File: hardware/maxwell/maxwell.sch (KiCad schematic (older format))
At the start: 48 parts, among them J1 Canbus 1, J10 SPI2_B, J11 BACKUP, J12 UART4, J15 I2C1, J16 ESP_BM, J17 ESP_PROG, J2 SPI2_C, J20 Interconnect (uC), J3 Neopixel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

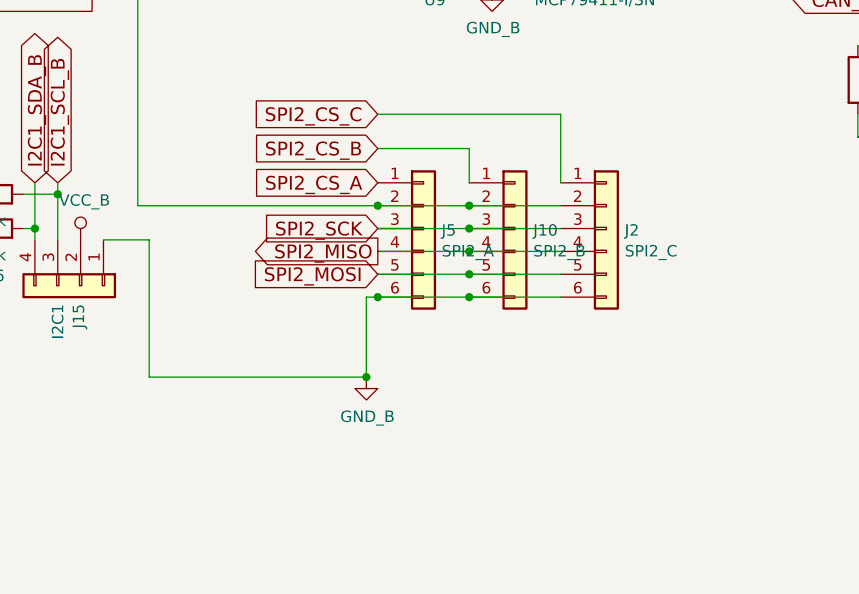
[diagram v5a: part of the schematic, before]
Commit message: Maxwell v1.9.6
Adapting main uC board such that it can serve for _both_ the
remote and main sides.  I'm printing a new case that can be mounted on
the front rack of the bike instead of the rear; this would obviate the
need for having two separate microcontrollers communicating over CAN.

* Adds new DISP connector in place of SPI_C (currently unused).
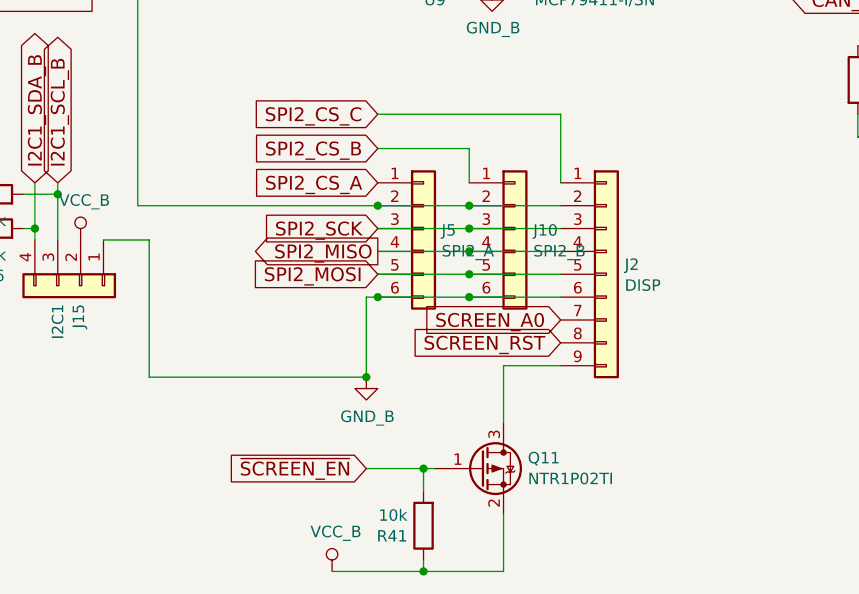
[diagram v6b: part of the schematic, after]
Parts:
- removed J2: SPI2_C, coddingtonbear:JST_XH_B06B-XH-A_06x2.50mm_Straight_LargePads, symbol maxwell-rescue:Conn_01x06-conn
- added J2: DISP, coddingtonbear:JST_XH_B09B-XH-A_1x09_P2.50mm_Straight_LargePads, symbol Connector_Generic:Conn_01x09
- added Q11: NTR1P02TI, coddingtonbear:SOT-23_LargePads, symbol Device:Q_PMOS_GSD
- added R41: 10k, coddingtonbear:0805_Milling, symbol maxwell-rescue:R-RESCUE-maxwell
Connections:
- net GND_B: now also J2.6 (Pin_6)
- net SPI2_CS_C: now also J2.1 (Pin_1)
- net SPI2_MISO: now also J2.4 (Pin_4)
- net SPI2_MOSI: now also J2.5 (Pin_5)
- net SPI2_SCK: now also J2.3 (Pin_3)
- net VCC_B: now also Q11.2 (S), R41.1
- net at J10.2 (Pin_2), J5.2 (Pin_2), U21.1 (DRAIN)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: now also J2.2 (Pin_2)
- new net: J2.9 (Pin_9), Q11.3 (D)
- new net SCREEN_A0: J2.7 (Pin_7)
- new net SCREEN_RST: J2.8 (Pin_8)
- new net ~SCREEN_EN: Q11.1 (G), R41.2
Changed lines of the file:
@@
 NoConn ~ 9450 3350
 NoConn ~ 9550 3350
-$Comp
-L maxwell-rescue:Conn_01x06-conn J2
-U 1 1 5BFB23A5
-P 6350 5500
-F 0 "J2" H 6430 5492 50  0000 L CNN
-F 1 "SPI2_C" H 6430 5401 50  0000 L CNN
-F 2 "coddingtonbear:JST_XH_B06B-XH-A_06x2.50mm_Straight_LargePads" H 6350 5500 50  0001 C CNN
-F 3 "~" H 6350 5500 50  0001 C CNN
-	1    6350 5500
-	1    0    0    -1
-$EndComp
 Wire Wire Line
 	5750 5400 6150 5400
@@
 Wire Wire Line
 	4600 3750 4600 4150
+$Comp
+L Connector_Generic:Conn_01x09 J2
+U 1 1 5CC5BE53
+P 6350 5700
+F 0 "J2" H 6430 5742 50  0000 L CNN
+F 1 "DISP" H 6430 5651 50  0000 L CNN
+F 2 "coddingtonbear:JST_XH_B09B-XH-A_1x09_P2.50mm_Straight_LargePads" H 6350 5700 50  0001 C CNN
+F 3 "~" H 6350 5700 50  0001 C CNN
+	1    6350 5700
+	1    0    0    -1
+$EndComp
+Text GLabel 6150 5900 0    60   Input ~ 0
+SCREEN_A0
+Text GLabel 6150 6000 0    60   Input ~ 0
+SCREEN_RST
+$Comp
+L Device:Q_PMOS_GSD Q11
+U 1 1 5CC5E136
+P 5800 6550
+F 0 "Q11" H 6006 6596 50  0000 L CNN
+F 1 "NTR1P02TI" H 6006 6505 50  0000 L CNN
+F 2 "coddingtonbear:SOT-23_LargePads" H 6000 6650 50  0001 C CNN
+F 3 "~" H 5800 6550 50  0001 C CNN
+	1    5800 6550
+	1    0    0    -1
+$EndComp
+Text GLabel 5300 6550 0    60   Input ~ 0
+~SCREEN_EN
+$Comp
+L maxwell-rescue:R-RESCUE-maxwell R41
+U 1 1 5CC5F256
+P 5550 6800
+F 0 "R41" H 5620 6846 50  0000 L CNN
+F 1 "10k" H 5620 6755 50  0000 L CNN
+F 2 "coddingtonbear:0805_Milling" V 5480 6800 50  0001 C CNN
+F 3 "" H 5550 6800 50  0001 C CNN
+	1    5550 6800
+	-1   0    0    1
+$EndComp
+Wire Wire Line
+	5900 6750 5900 7000
+Wire Wire Line
+	5900 7000 5550 7000
+Wire Wire Line
+	5600 6550 5550 6550
+Wire Wire Line
+	5550 6650 5550 6550
+Connection ~ 5550 6550
+Wire Wire Line
+	5550 6550 5300 6550
+Wire Wire Line
+	5550 6950 5550 7000
+Connection ~ 5550 7000
+Wire Wire Line
+	5550 7000 5150 7000
+Wire Wire Line
+	6150 6100 5900 6100
+Wire Wire Line
+	5900 6100 5900 6350
+$Comp
+L coddingtonbear:VCC_B #PWR?
+U 1 1 5CCA1B6F
+P 5150 7000
+F 0 "#PWR?" H 5150 6850 50  0001 C CNN
+F 1 "VCC_B" H 5167 7173 50  0000 C CNN
+F 2 "" H 5150 7000 50  0001 C CNN
+F 3 "" H 5150 7000 50  0001 C CNN
+	1    5150 7000
+	1    0    0    -1
+$EndComp
 $EndSCHEMATC

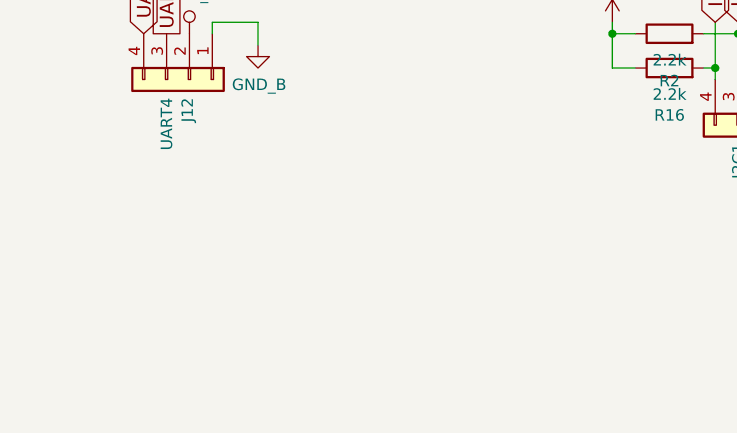
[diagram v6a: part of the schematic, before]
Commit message: Maxwell v1.9.7
Forgot to add connectors for left/right control sets.

* Adds connectors for LEFT_A/B and RIGHT_A/B
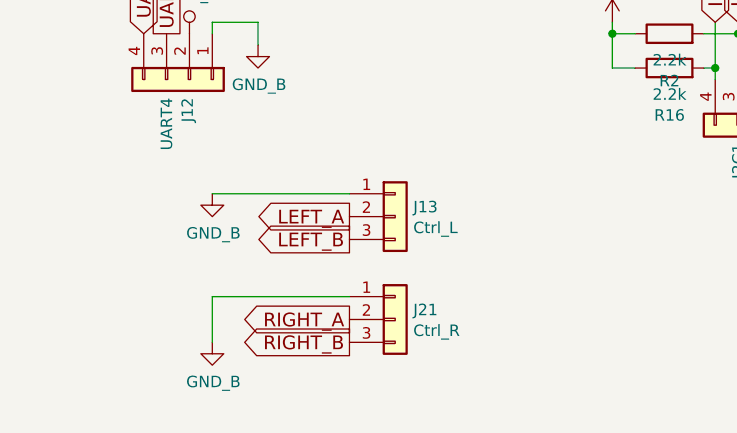
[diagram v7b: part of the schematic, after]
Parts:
- added J13: Ctrl_L, coddingtonbear:JST_XH_B03B-XH-A_03x2.50mm_Straight_LargePads, symbol Connector_Generic:Conn_01x03
- added J21: Ctrl_R, coddingtonbear:JST_XH_B03B-XH-A_03x2.50mm_Straight_LargePads, symbol Connector_Generic:Conn_01x03
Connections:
- net GND_B: now also J13.1 (Pin_1), J21.1 (Pin_1)
- new net LEFT_A: J13.2 (Pin_2)
- new net LEFT_B: J13.3 (Pin_3)
- new net RIGHT_A: J21.2 (Pin_2)
- new net RIGHT_B: J21.3 (Pin_3)
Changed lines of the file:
@@
 	5900 6100 5900 6350
 $Comp
-L coddingtonbear:VCC_B #PWR?
+L coddingtonbear:VCC_B #PWR0194
 U 1 1 5CCA1B6F
 P 5150 7000
-F 0 "#PWR?" H 5150 6850 50  0001 C CNN
+F 0 "#PWR0194" H 5150 6850 50  0001 C CNN
 F 1 "VCC_B" H 5167 7173 50  0000 C CNN
 F 2 "" H 5150 7000 50  0001 C CNN
@@
 	1    0    0    -1
 $EndComp
+$Comp
+L Connector_Generic:Conn_01x03 J13
+U 1 1 5CCAEC45
+P 2450 6150
+F 0 "J13" H 2529 6192 50  0000 L CNN
+F 1 "Ctrl_L" H 2529 6101 50  0000 L CNN
+F 2 "coddingtonbear:JST_XH_B03B-XH-A_03x2.50mm_Straight_LargePads" H 2450 6150 50  0001 C CNN
+F 3 "~" H 2450 6150 50  0001 C CNN
+	1    2450 6150
+	1    0    0    -1
+$EndComp
+$Comp
+L Connector_Generic:Conn_01x03 J21
+U 1 1 5CCAED15
+P 2450 6600
+F 0 "J21" H 2529 6642 50  0000 L CNN
+F 1 "Ctrl_R" H 2529 6551 50  0000 L CNN
+F 2 "coddingtonbear:JST_XH_B03B-XH-A_03x2.50mm_Straight_LargePads" H 2450 6600 50  0001 C CNN
+F 3 "~" H 2450 6600 50  0001 C CNN
+	1    2450 6600
+	1    0    0    -1
+$EndComp
+$Comp
+L coddingtonbear:GND_B #PWR0195
+U 1 1 5CCAF046
+P 1650 6050
+F 0 "#PWR0195" H 1650 5800 50  0001 C CNN
+F 1 "GND_B" H 1655 5877 50  0000 C CNN
+F 2 "" H 1650 6050 50  0001 C CNN
+F 3 "" H 1650 6050 50  0001 C CNN
+	1    1650 6050
+	1    0    0    -1
+$EndComp
+$Comp
+L coddingtonbear:GND_B #PWR0196
+U 1 1 5CCAF0B9
+P 1650 6700
+F 0 "#PWR0196" H 1650 6450 50  0001 C CNN
+F 1 "GND_B" H 1655 6527 50  0000 C CNN
+F 2 "" H 1650 6700 50  0001 C CNN
+F 3 "" H 1650 6700 50  0001 C CNN
+	1    1650 6700
+	1    0    0    -1
+$EndComp
+Text GLabel 2250 6150 0    60   Output ~ 0
+LEFT_A
+Text GLabel 2250 6250 0    60   Output ~ 0
+LEFT_B
+Text GLabel 2250 6600 0    60   Output ~ 0
+RIGHT_A
+Text GLabel 2250 6700 0    60   Output ~ 0
+RIGHT_B
+Wire Wire Line
+	2250 6050 1650 6050
+Wire Wire Line
+	2250 6500 1650 6500
+Wire Wire Line
+	1650 6500 1650 6700
 $EndSCHEMATC

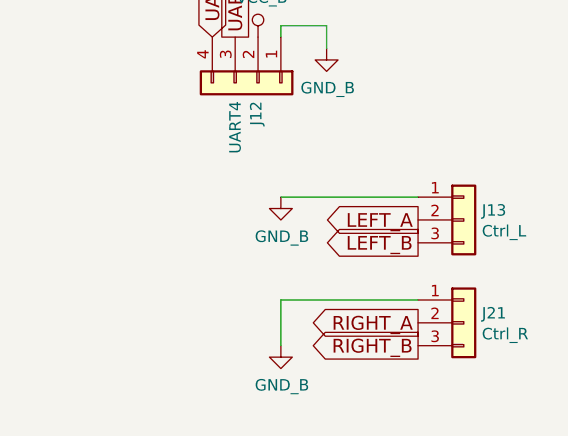
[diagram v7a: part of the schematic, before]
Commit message: Added WAKE adapter board; began layout for new power board.
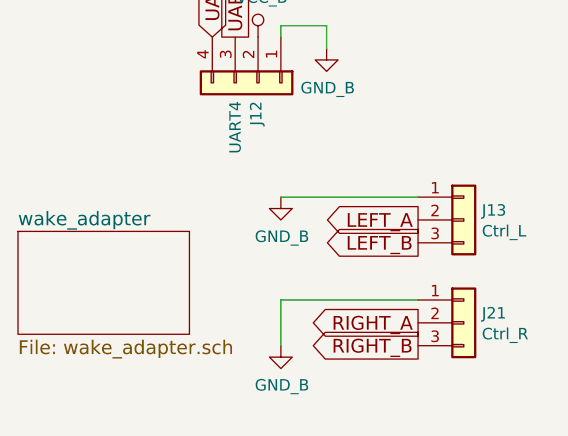
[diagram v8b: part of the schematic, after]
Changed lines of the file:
@@
 $Descr A4 11693 8268
 encoding utf-8
-Sheet 1 4
+Sheet 1 5
 Title ""
 Date ""
@@
 Wire Wire Line
 	1650 6500 1650 6700
+$Sheet
+S 500  6200 750  450
+U 5CD4044C
+F0 "wake_adapter" 60
+F1 "wake_adapter.sch" 60
+$EndSheet
 $EndSCHEMATC
